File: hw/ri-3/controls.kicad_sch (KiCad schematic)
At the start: 17 parts, among them Q1 MMBT3904, Q13 2N7002, Q2 MMBT3904

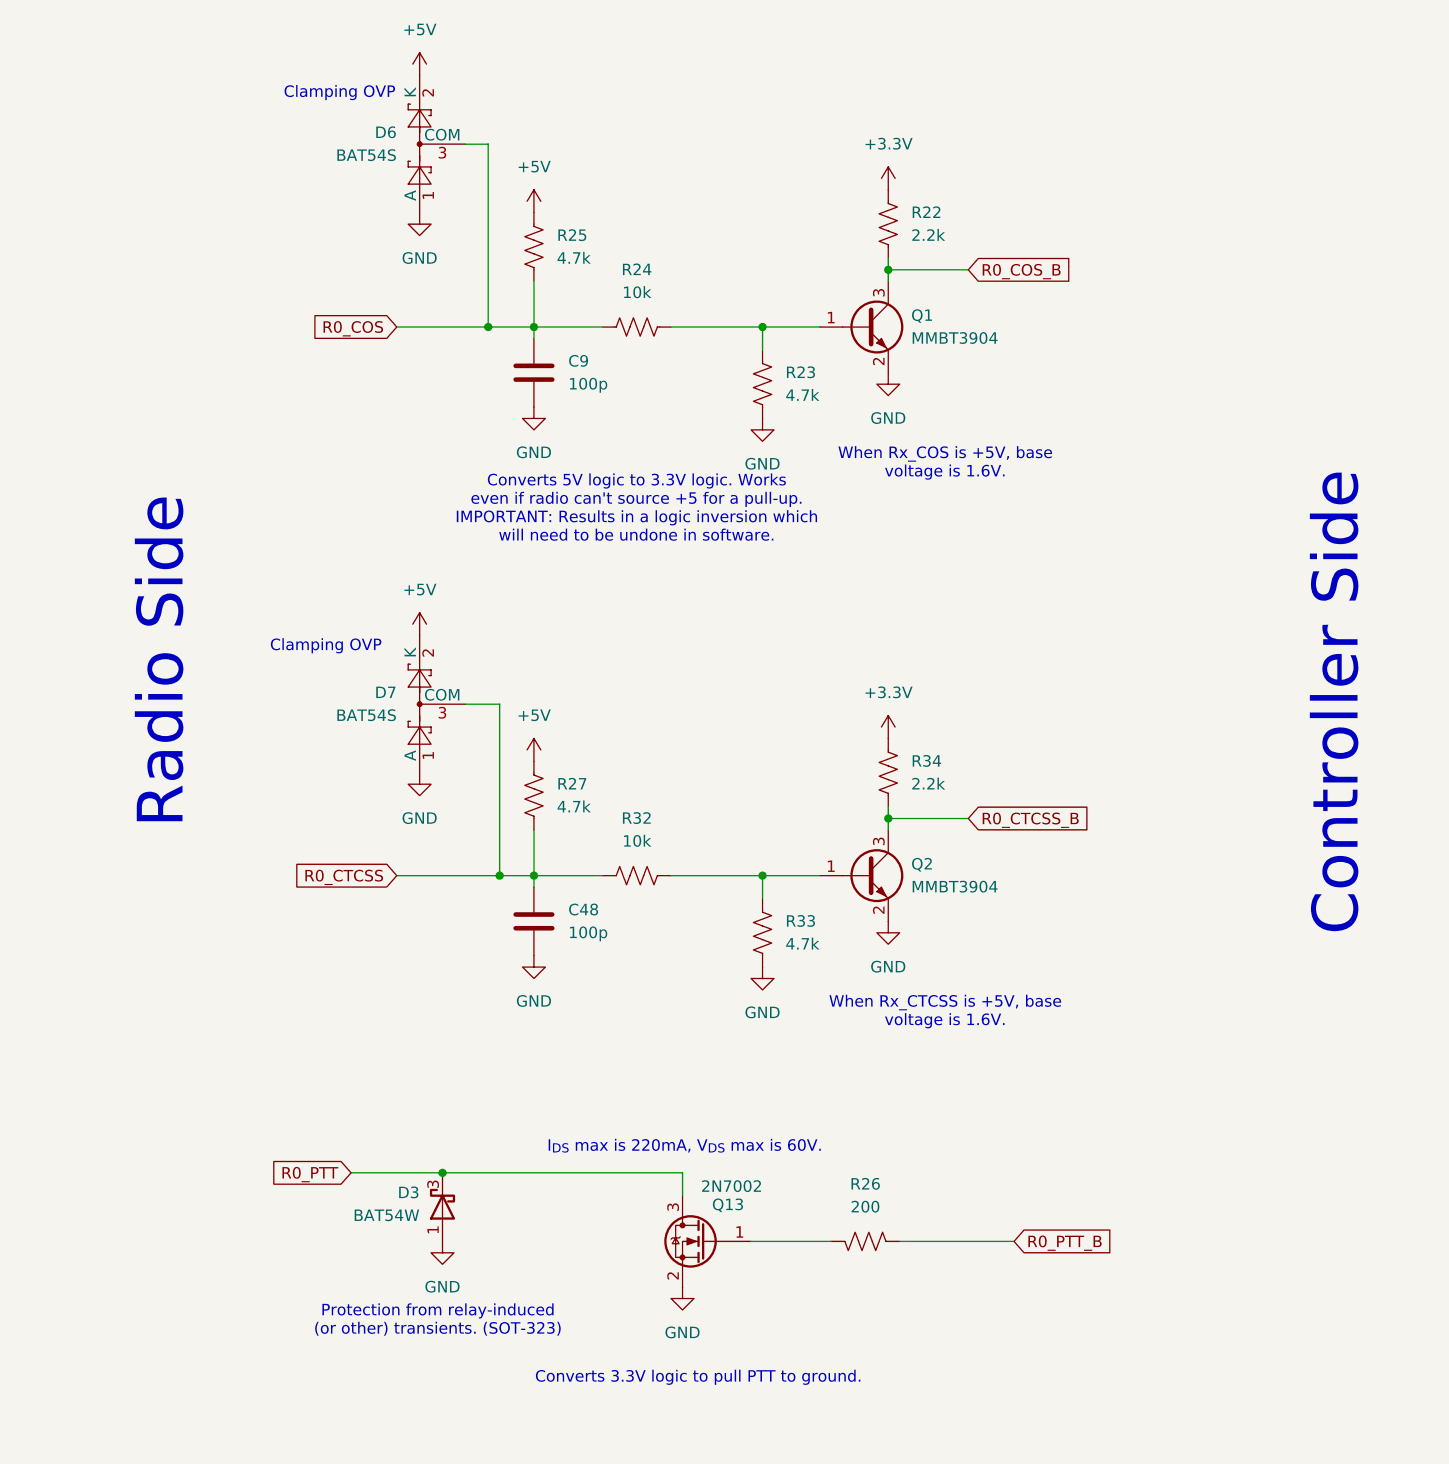
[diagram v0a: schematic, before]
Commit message: Updating schematics, create new mini-board for radio interface
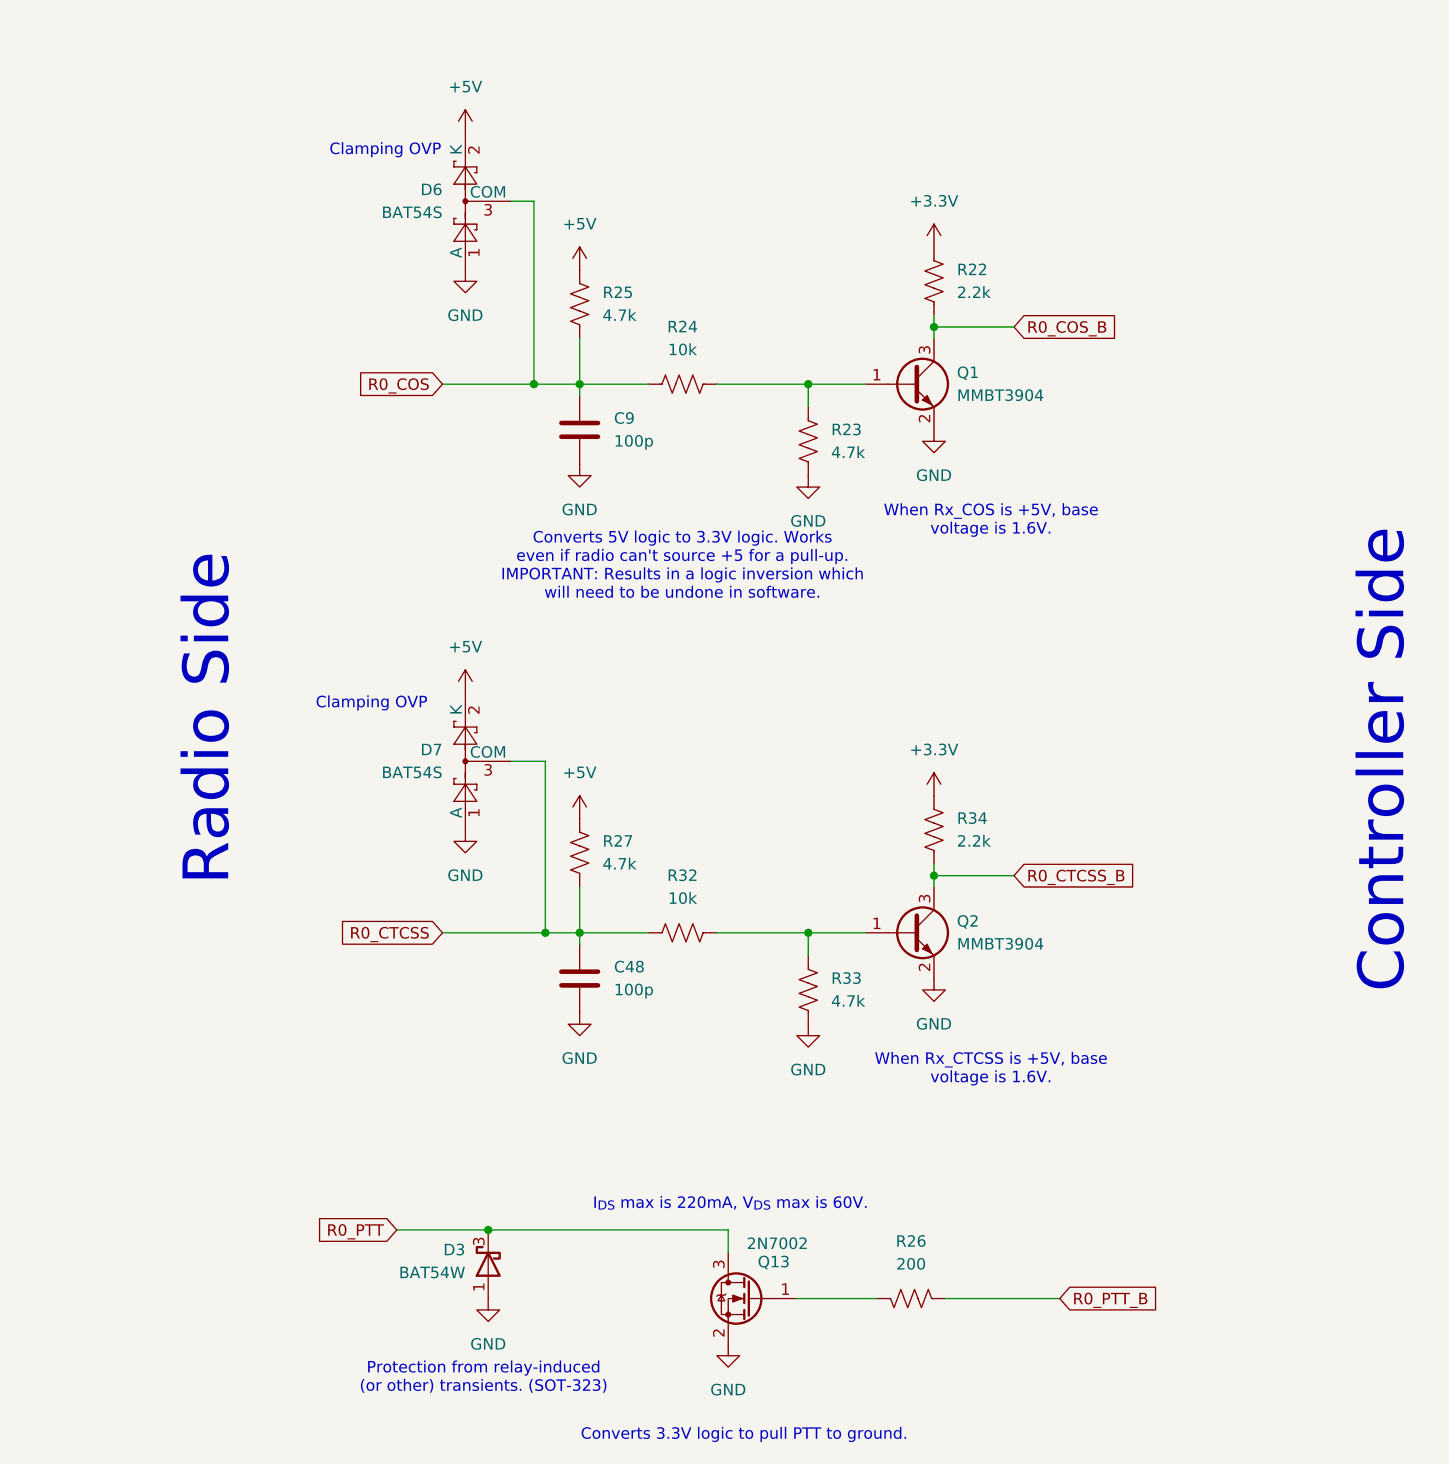
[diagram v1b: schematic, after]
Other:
- company: Bruce MacKinnon KC1FSZ -> (none)
- title: COS/CTCSS/PTT Controls (Radio 0) -> (none)
- moved on the sheet: C48, C9, D3, D6, D7, Q1, Q13, Q2, R22, R23, R24, R25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

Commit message: Updating schematics, create new mini-board for radio interface
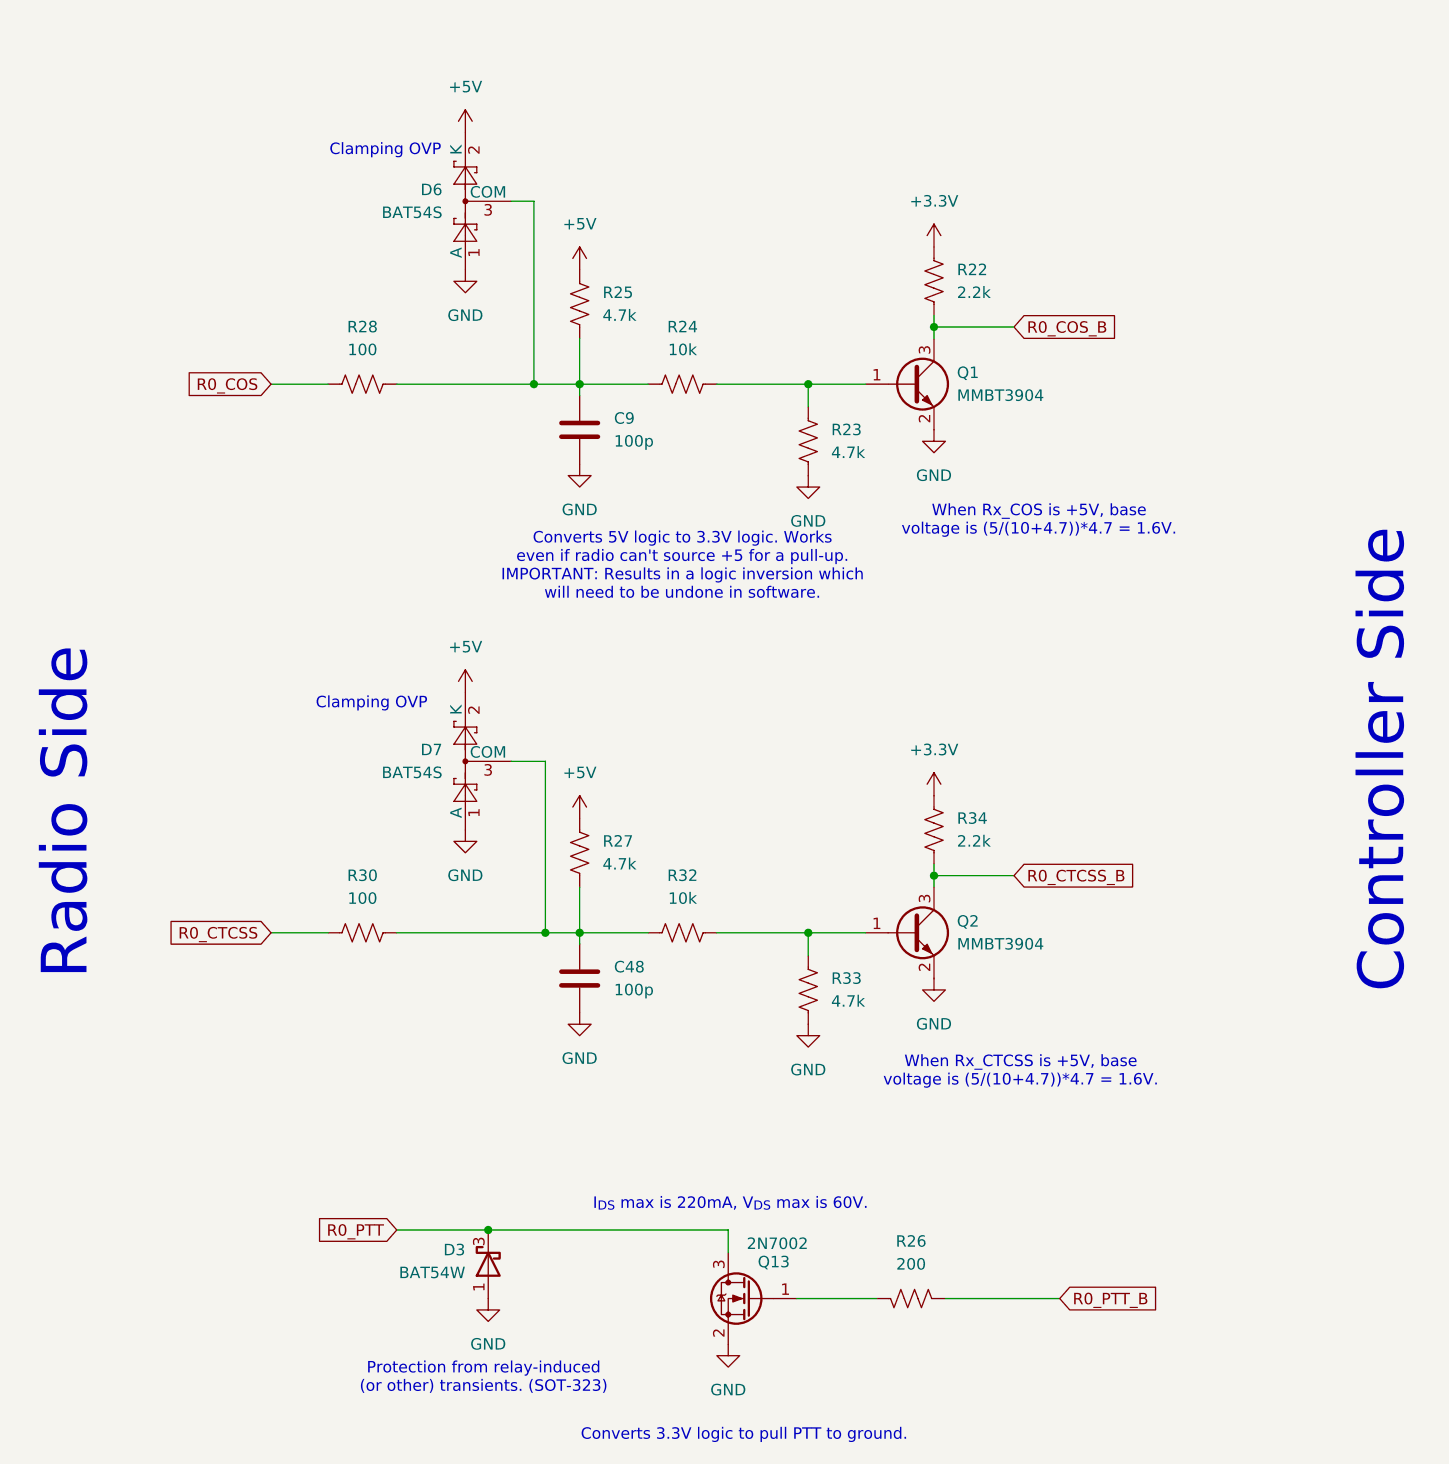
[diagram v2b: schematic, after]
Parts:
- added R28, R30: 100, Resistor_SMD:R_0805_2012Metric_Pad1.20x1.40mm_HandSolder, symbol Device:R_US
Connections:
- net R0_COS: now also R28.1; no longer C9.1, D6.3 (COM), R24.1, R25.2
- net R0_CTCSS: now also R30.1; no longer C48.1, D7.3 (COM), R27.2, R32.1
- new net: C9.1, D6.3 (COM), R24.1, R25.2, R28.2
- new net: C48.1, D7.3 (COM), R27.2, R30.2, R32.1
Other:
- note added: "When Rx_COS is +5V, base voltage is (5/(10+4.7))*4.7 = 1.6V."
- note added: "When Rx_CTCSS is +5V, base voltage is (5/(10+4.7))*4.7 = 1.6V."
- note removed: "When Rx_COS is +5V, base voltage is 1.6V."
- note removed: "When Rx_CTCSS is +5V, base voltage is 1.6V."
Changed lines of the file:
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@@
 		)
 	)
-	(text "When Rx_COS is +5V, base \nvoltage is 1.6V."
-		(exclude_from_sim no)
-		(at 156.21 68.58 0)
+	(text "When Rx_COS is +5V, base \nvoltage is (5/(10+4.7))*4.7 = 1.6V.\n"
+		(exclude_from_sim no)
+		(at 161.544 68.58 0)
 		(effects
 			(font
 				(size 1.27 1.27)
-			)
-		)
-	)
-	(text "When Rx_CTCSS is +5V, base \nvoltage is 1.6V."
-		(exclude_from_sim no)
-		(at 156.21 129.54 0)
+				(color 255 5 238 1)
+			)
+		)
+	)
+	(text "When Rx_CTCSS is +5V, base \nvoltage is (5/(10+4.7))*4.7 = 1.6V.\n"
+		(exclude_from_sim no)
+		(at 159.512 129.794 0)
 		(effects
 			(font
 				(size 1.27 1.27)
+				(color 255 5 238 1)
 			)
 		)
@@
 	(text "Radio Side"
 		(exclude_from_sim no)
-		(at 69.088 90.678 90)
+		(at 53.34 101.092 90)
 		(effects
 			(font
@@
 	(wire
 		(pts
+			(xy 90.17 53.34) (xy 105.41 53.34)
+		)
+		(stroke
+			(width 0)
+			(type default)
+		)
+	)
+	(wire
+		(pts
 			(xy 149.86 46.99) (xy 158.75 46.99)
 		)
@@
 	(wire
 		(pts
-			(xy 105.41 53.34) (xy 95.25 53.34)
-		)
-		(stroke
-			(width 0)
-			(type default)
-		)
-	)
-	(wire
-		(pts
 			(xy 110.49 114.3) (xy 118.11 114.3)
 		)
@@
 	(wire
 		(pts
+			(xy 76.2 53.34) (xy 82.55 53.34)
+		)
+		(stroke
+			(width 0)
+			(type default)
+		)
+	)
+	(wire
+		(pts
 			(xy 149.86 107.95) (xy 158.75 107.95)
 		)
@@
 	(wire
 		(pts
+			(xy 90.17 114.3) (xy 106.68 114.3)
+		)
+		(stroke
+			(width 0)
+			(type default)
+		)
+	)
+	(wire
+		(pts
 			(xy 110.49 48.26) (xy 110.49 53.34)
 		)
@@
 	(wire
 		(pts
-			(xy 106.68 114.3) (xy 95.25 114.3)
+			(xy 76.2 114.3) (xy 82.55 114.3)
 		)
 		(stroke
@@
 	(global_label "R0_CTCSS"
 		(shape input)
-		(at 95.25 114.3 180)
+		(at 76.2 114.3 180)
 		(fields_autoplaced yes)
 		(effects
@@
 		)
 		(property "Intersheetrefs" "${INTERSHEET_REFS}"
-			(at 82.8911 114.3 0)
+			(at 63.8411 114.3 0)
 			(effects
 				(font
@@
 	(global_label "R0_COS"
 		(shape input)
-		(at 95.25 53.34 180)
+		(at 76.2 53.34 180)
 		(fields_autoplaced yes)
 		(effects
@@
 		)
 		(property "Intersheetrefs" "${INTERSHEET_REFS}"
-			(at 85.0077 53.34 0)
+			(at 65.9577 53.34 0)
 			(effects
 				(font
@@
 	)
 	(symbol
+		(lib_id "Device:R_US")
+		(at 86.36 114.3 90)
+		(unit 1)
+		(exclude_from_sim no)
+		(in_bom yes)
+		(on_board yes)
+		(dnp no)
+		(property "Reference" "R30"
+			(at 86.36 107.95 90)
+			(effects
+				(font
+					(size 1.27 1.27)
+				)
+			)
+		)
+		(property "Value" "100"
+			(at 86.36 110.49 90)
+			(effects
+				(font
+					(size 1.27 1.27)
+				)
+			)
+		)
+		(property "Footprint" "Resistor_SMD:R_0805_2012Metric_Pad1.20x1.40mm_HandSolder"
+			(at 86.614 113.284 90)
+			(effects
+				(font
+					(size 1.27 1.27)
+				)
+				(hide yes)
+			)
+		)
+		(property "Datasheet" "~"
+			(at 86.36 114.3 0)
+			(effects
+				(font
+					(size 1.27 1.27)
+				)
+				(hide yes)
+			)
+		)
+		(property "Description" "Resistor, US symbol"
+			(at 86.36 114.3 0)
+			(effects
+				(font
+					(size 1.27 1.27)
+				)
+				(hide yes)
+			)
+		)
+		(pin "2"
+		)
+		(pin "1"
+		)
+		(instances
+			(project "ri-3"
+				(path "/110f0872-f0f3-48d7-8cc0-6d84dcccd4c0/0ec0339f-187c-413f-a3a3-b497acd59b98"
+					(reference "R30")
+					(unit 1)
+				)
+			)
+		)
+	)
+	(symbol
 		(lib_id "Diode:BAT54W")
 		(at 100.33 151.13 90)
@@
 					(unit 1)
 				)
+			)
+		)
+	)
+	(symbol
+		(lib_id "Device:R_US")
+		(at 86.36 53.34 90)
+		(unit 1)
+		(exclude_from_sim no)
+		(in_bom yes)
+		(on_board yes)
+		(dnp no)
+		(property "Reference" "R28"
+			(at 86.36 46.99 90)
+			(effects
+				(font
+					(size 1.27 1.27)
+				)
+			)
+		)
+		(property "Value" "100"
+			(at 86.36 49.53 90)
+			(effects
+				(font
+					(size 1.27 1.27)
+				)
+			)
+		)
+		(property "Footprint" "Resistor_SMD:R_0805_2012Metric_Pad1.20x1.40mm_HandSolder"
+			(at 86.614 52.324 90)
+			(effects
+				(font
+					(size 1.27 1.27)
+				)
+				(hide yes)
+			)
+		)
+		(property "Datasheet" "~"
+			(at 86.36 53.34 0)
+			(effects
+				(font
+					(size 1.27 1.27)
+				)
+				(hide yes)
+			)
+		)
+		(property "Description" "Resistor, US symbol"
+			(at 86.36 53.34 0)
+			(effects
+				(font
+					(size 1.27 1.27)
+				)
+				(hide yes)
+			)
+		)
+		(pin "2"
+		)
+		(pin "1"
+		)
+		(instances
+			(project "ri-3"
+				(path "/110f0872-f0f3-48d7-8cc0-6d84dcccd4c0/0ec0339f-187c-413f-a3a3-b497acd59b98"
+					(reference "R28")
+					(unit 1)
+				)
